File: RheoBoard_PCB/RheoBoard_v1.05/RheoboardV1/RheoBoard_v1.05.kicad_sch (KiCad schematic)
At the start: 165 parts, among them J1 JST SH 4-pin 1.00mm, J12 JST SH 4-pin 1.00mm, J17 JST SH 4-pin 1.00mm, J2 PJ-082BH, J3 JST EH 4-pin 2.50mm, J9 JST SH 4-pin 1.00mm, Q10 AO3400A, Q3 AO3400A, Q4 AO3400A, Q8 AO3400A, SW1 TL3301NF160QG/P010515, SW2 TL3301NF160QG/P010515, SW3 TL3301NF160QG/P010515, SW4 TL3301NF160QG/P010515, U1 TPS563203DRLR, U10 JST XH 2-pin 2.50mm, U11 ZR370-02PM / 4.5V / 2.5 LPM /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, U12 TPS259472ARPWR, U13 TCA9517ADGKR, U2 TPS563203DRLR, U3 TPS563203DRLR, U4 TCA9534APWR, U5 MPRLS0025PA00001A, U7 PCA9685PW,118, U8 ZR370-02PM / 4.5V / 2.5 LPM /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, U9 JST XH 2-pin 2.50mm

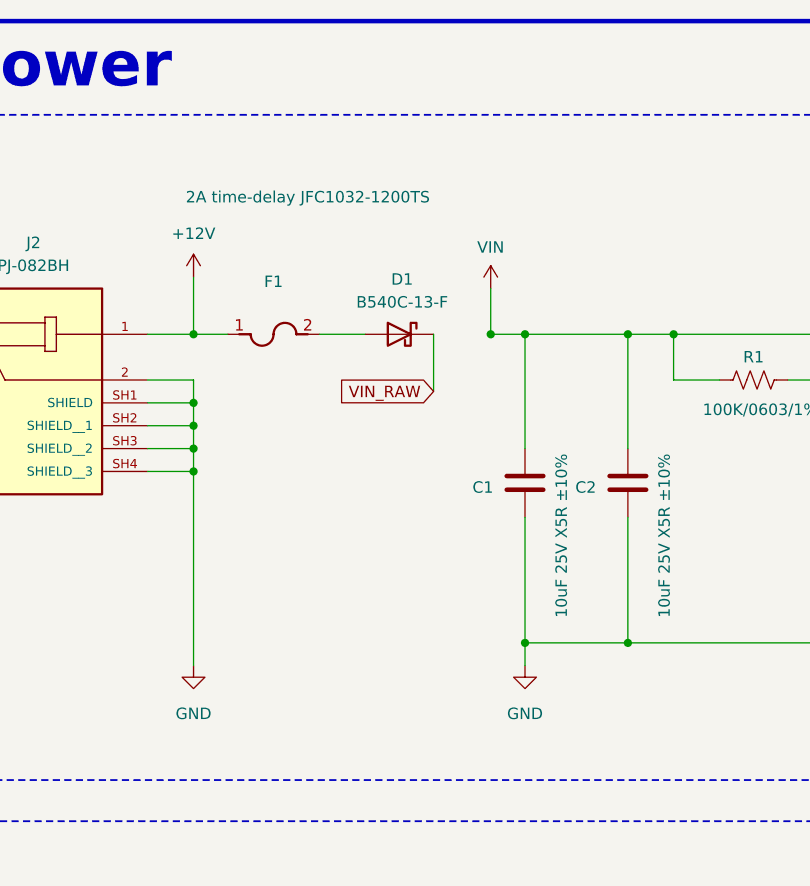
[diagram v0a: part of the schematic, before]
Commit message: Update RheoBoard design files and documentation
- Modified column widths and sorting column in the Altium reimport file for better layout management.
- Added a new P-MOSFET symbol with detailed properties to the schematic for enhanced component representation.
- Updated documentation to clarify the structure and content of the PCB section, including a new block diagram and revised image references.

These changes improve the clarity and usability of the RheoBoard project files and documentation.
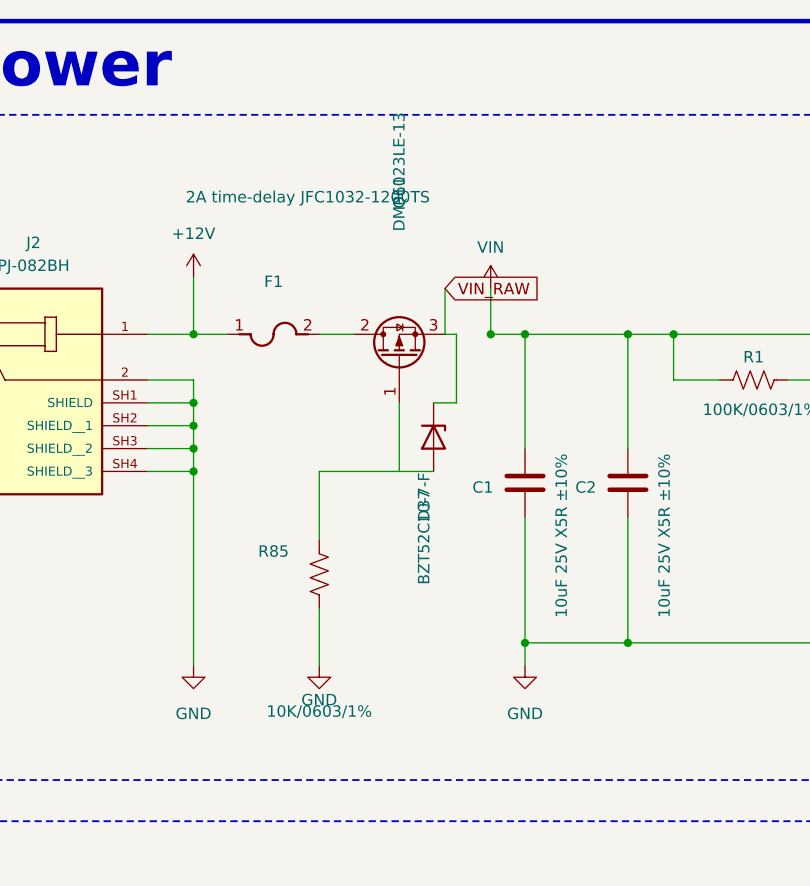
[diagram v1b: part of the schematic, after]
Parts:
- removed D1: B540C-13-F, Diode_SMD:D_SMC, symbol Device:D_Schottky
- added D37: BZT52C10-7-F, Diode_SMD:D_SOD-123, symbol Device:D_Zener
- added Q11: DMP6023LE-13, Package_TO_SOT_SMD:SOT-223-3_TabPin2, symbol Transistor_FET:Q_PMOS_GDS
- added R85: 10K/0603/1%, Resistor_SMD:R_0603_1608Metric_Pad0.98x0.95mm_HandSolder, symbol Device:R_US
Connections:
- net GND: now also R85.2
- net VIN_RAW: now also D37.1 (K), Q11.3 (S)
- net at F1.2: now also Q11.2 (D)
- new net: D37.2 (A), Q11.1 (G), R85.1

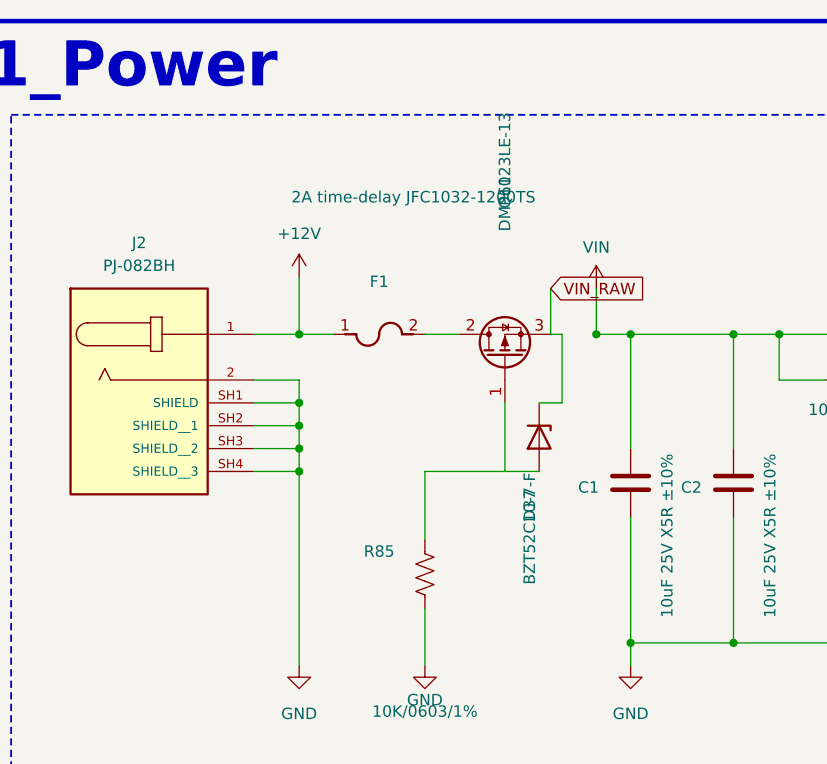
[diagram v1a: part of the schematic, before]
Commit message: Update RheoBoard design files and documentation
- Renamed schematic and PCB file references for consistency across the project.
- Added a new SOD-123 diode footprint with detailed properties, including a datasheet link and assembly information.
- Adjusted global labels and junctions in the schematic for improved clarity and accuracy.
- Updated image dimensions in documentation for better presentation.

These changes enhance the organization, usability, and clarity of the RheoBoard project files and documentation.
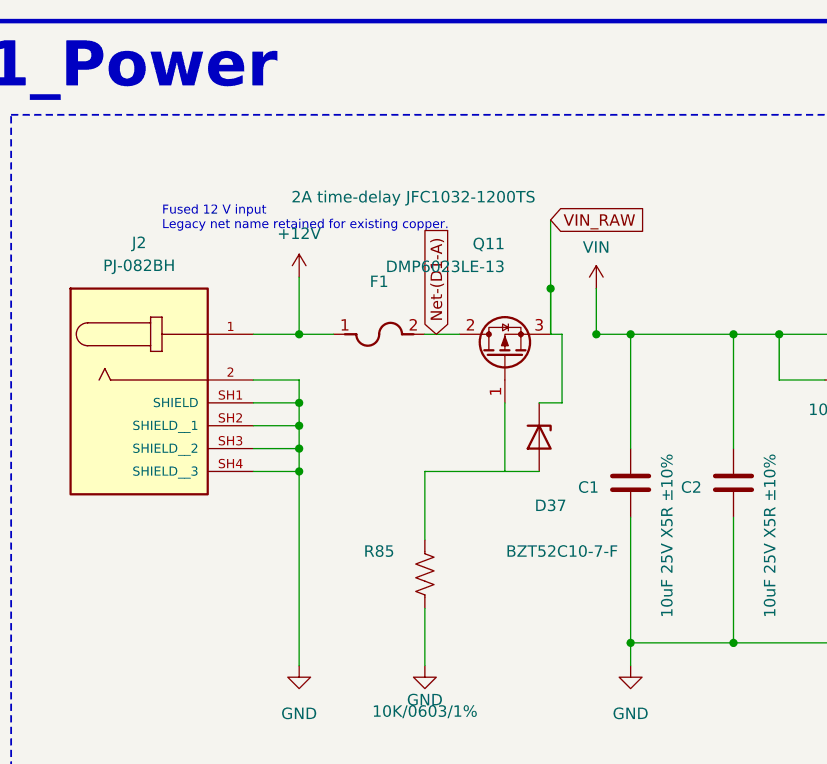
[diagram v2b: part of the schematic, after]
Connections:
- net Net-(D1-A): now reaches F1.2, Q11.2 (D)
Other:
- note added: "Fused 12 V input Legacy net name retained for existing copper."
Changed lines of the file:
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@@
 		(diameter 0)
 	)
+	(junction
+		(at 100.33 60.96)
+		(diameter 0)
+	)
 	(no_connect
 		(at 683.26 419.1)
@@
 		)
 	)
+	(wire
+		(pts
+			(xy 100.33 66.04)
+			(xy 100.33 53.34)
+		)
+	)
 	(text "BUCK 12V - 3V3\n\n"
 		(at 168.656 206.502 0)
@@
 		)
 	)
+	(global_label "Net-(D1-A)"
+		(shape input)
+		(at 87.63 66.04 90)
+		(effects
+			(font
+				(size 1.27 1.27)
+			)
+			(justify left)
+		)
+	)
 	(global_label "VIN_RAW"
 		(shape input)
-		(at 100.33 60.96 0)
+		(at 100.33 53.34 0)
 		(effects
 			(font
@@
 		)
 	)
+  (text "Fused 12 V input\nLegacy net name retained for existing copper."
+    (at 57.15 54.61 0)
+    (effects (font (size 1 1)) (justify left bottom))
+  )
 	(symbol
 		(lib_id "Mechanical:MountingHole")
@@
 		(dnp no)
 		(property "Reference" "Q11"
-			(at 95.25 52.07 0)
+			(at 95.25 56 90)
 			(effects
 				(font
@@
 		)
 		(property "Value" "DMP6023LE-13"
-			(at 95.25 54.61 0)
+			(at 95.25 58.54 90)
 			(effects
 				(font
@@
 		(dnp no)
 		(property "Reference" "D37"
-			(at 98 85.09 0)
+			(at 100.33 85.09 90)
 			(effects
 				(font
@@
 		)
 		(property "Value" "BZT52C10-7-F"
-			(at 98 87.63 0)
+			(at 101.6 90.17 90)
 			(effects
 				(font

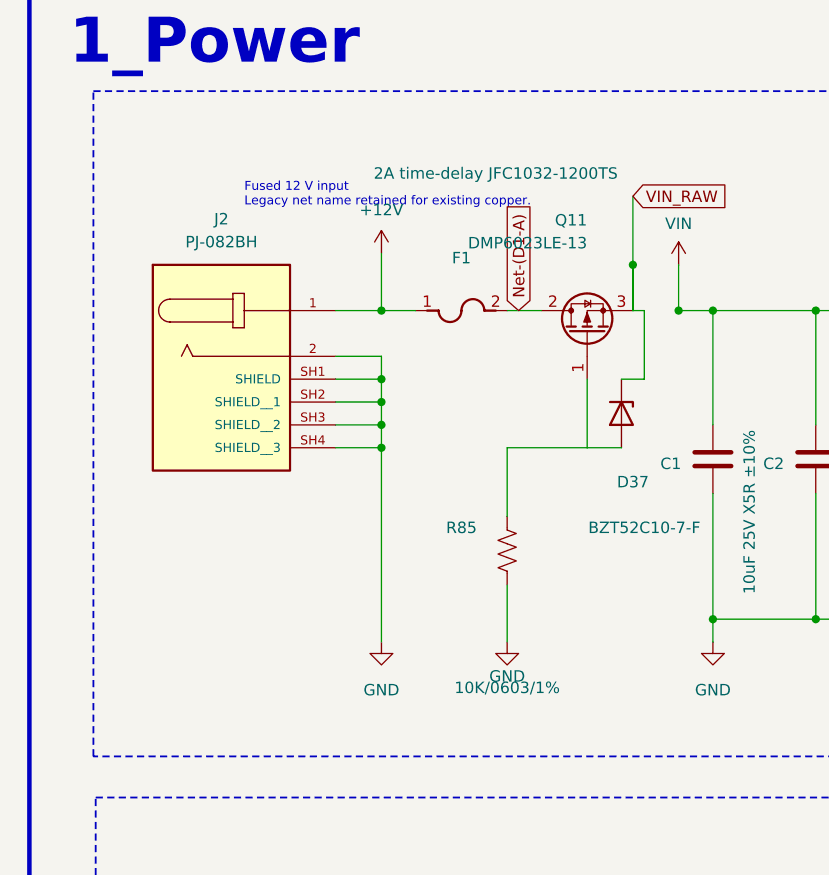
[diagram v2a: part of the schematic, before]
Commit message: Update RheoBoard PCB and schematic files for improved component alignment and clarity
- Adjusted the orientation and positioning of various properties for the SOD-123 diode footprint in the PCB file to ensure proper alignment.
- Added a new junction in the schematic and modified wire connections for better clarity and accuracy.
- Updated global labels to reflect changes in net names and improved layout consistency.

These changes enhance the usability and accuracy of the RheoBoard design files.
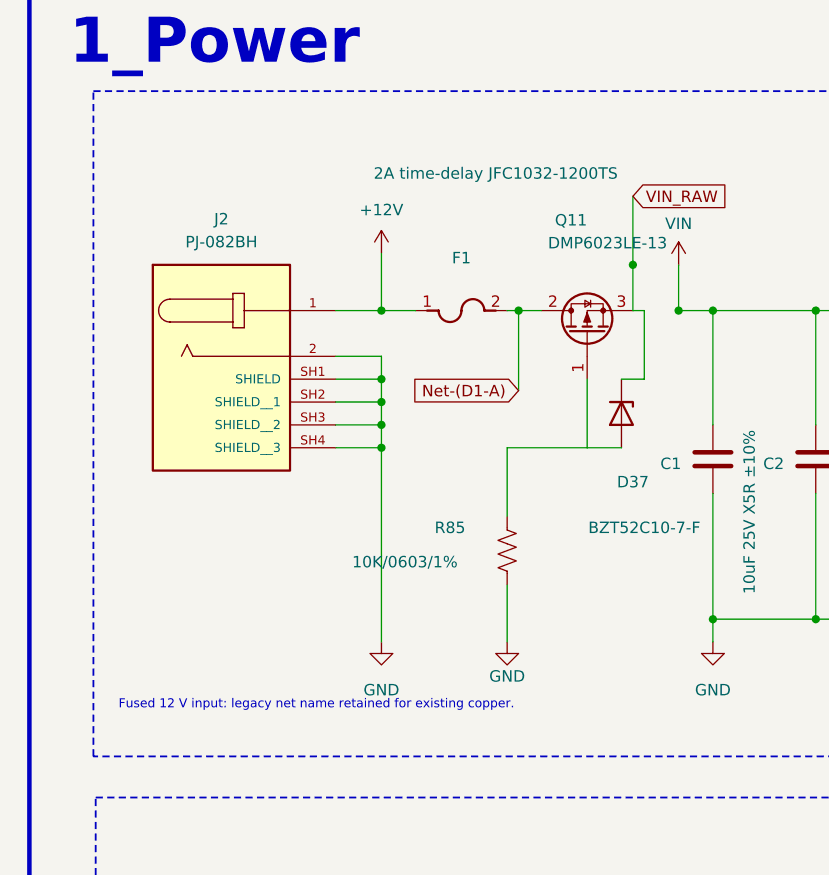
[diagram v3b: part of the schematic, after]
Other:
- note added: "Fused 12 V input: legacy net name retained for existing copper."
- note removed: "Fused 12 V input Legacy net name retained for existing copper."
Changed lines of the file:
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@@
 		(diameter 0)
 	)
+	(junction
+		(at 87.63 66.04)
+		(diameter 0)
+	)
 	(no_connect
 		(at 683.26 419.1)
@@
 		(pts
 			(xy 100.33 66.04)
-			(xy 100.33 60.96)
+			(xy 100.33 53.34)
 		)
 	)
 	(wire
 		(pts
-			(xy 100.33 66.04)
-			(xy 100.33 53.34)
+			(xy 87.63 66.04)
+			(xy 87.63 74.93)
 		)
 	)
@@
 		)
 	)
+	(text "Fused 12 V input: legacy net name retained for existing copper."
+		(at 43.18 110.49 0)
+		(effects
+			(font
+				(size 1 1)
+			)
+			(justify left bottom)
+		)
+	)
 	(label "EF_EN"
 		(at 358.14 162.56 180)
@@
 		)
 	)
-	(global_label "Net-(D1-A)"
+	(global_label "VIN_RAW"
 		(shape input)
-		(at 87.63 66.04 90)
+		(at 100.33 53.34 0)
 		(effects
 			(font
@@
 		)
 	)
-	(global_label "VIN_RAW"
+	(global_label "Net-(D1-A)"
 		(shape input)
-		(at 100.33 53.34 0)
+		(at 87.63 74.93 180)
 		(effects
 			(font
 				(size 1.27 1.27)
 			)
-			(justify left)
+			(justify right)
 		)
 	)
-  (text "Fused 12 V input\nLegacy net name retained for existing copper."
-    (at 57.15 54.61 0)
-    (effects (font (size 1 1)) (justify left bottom))
-  )
 	(symbol
 		(lib_id "Mechanical:MountingHole")
@@
 		)
 		(property "Value" "DMP6023LE-13"
-			(at 95.25 58.54 90)
+			(at 104.14 58.54 90)
 			(effects
 				(font
@@
 		(dnp no)
 		(property "Reference" "R85"
-			(at 81.28 90.17 0)
+			(at 80.01 90.17 0)
 			(effects
 				(font
@@
 		)
 		(property "Value" "10K/0603/1%"
-			(at 86.36 107.95 0)
+			(at 75 93.98 0)
 			(effects
 				(font
